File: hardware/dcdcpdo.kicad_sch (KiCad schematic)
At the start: 22 parts, among them J501 MANUAL, U301 SiC437

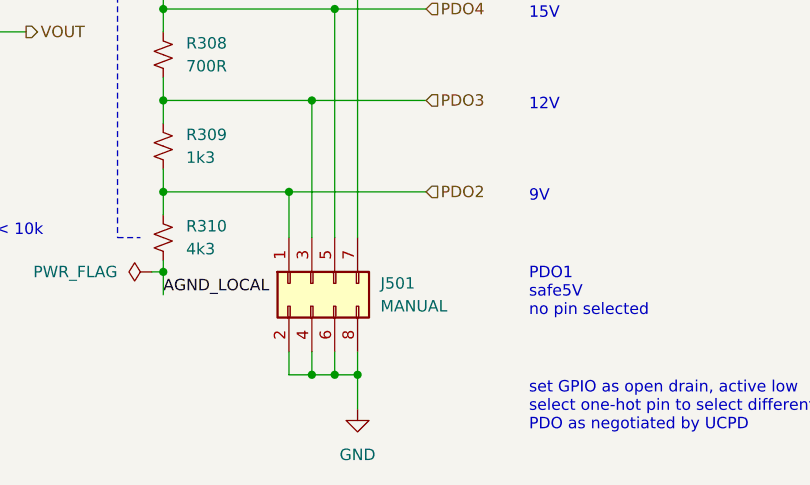
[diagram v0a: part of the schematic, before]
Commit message: Fix SiC437 footprint and LCSC field error
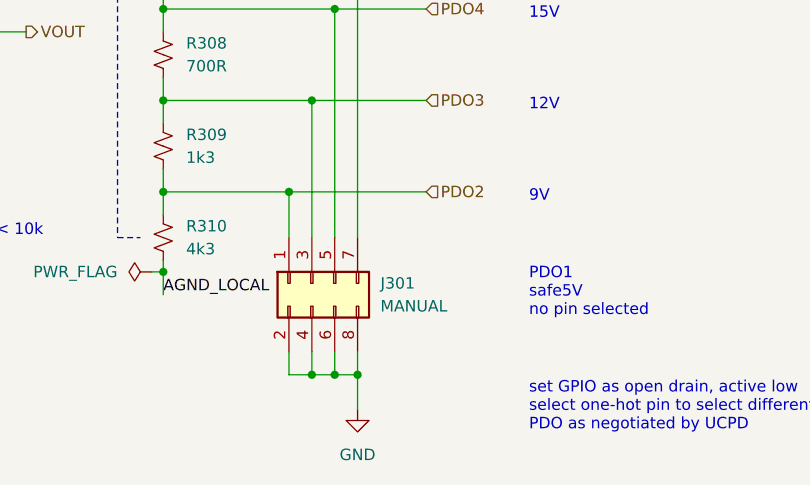
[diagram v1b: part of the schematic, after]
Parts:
- C301, C303: LCSC ID (none) -> C14663; LCSC Part C14663 -> (none)
- C302: LCSC ID (none) -> C45783; LCSC Part C45783 -> (none)
- C304: LCSC ID (none) -> C15849; LCSC Part C15849 -> (none)
- C305: LCSC ID (none) -> C19666; LCSC Part C19666 -> (none)
- C306, C307, C308, C309: LCSC ID (none) -> C76659; LCSC Part C76659 -> (none)
- J301: renamed from J501; LCSC ID (none) -> C2685182
- L301: LCSC ID (none) -> C524588; LCSC Part C524588 -> (none)
- R301: LCSC ID (none) -> C22939; LCSC Part C22939 -> (none)
- R302: LCSC ID (none) -> C25744; LCSC Part C25744 -> (none)
- R303: LCSC ID (none) -> C137971; LCSC Part C137971 -> (none)
- R304: LCSC ID (none) -> C25741; LCSC Part C25741 -> (none)
- R305: LCSC ID (none) -> C25794; LCSC Part C25794 -> (none)
- R306: LCSC ID (none) -> C4109; LCSC Part C4109 -> (none)
- R307, R308: LCSC ID (none) -> C728428; LCSC Part C728428 -> (none)
- R309: LCSC ID (none) -> C25866; LCSC Part C25866 -> (none)
- R310: LCSC ID (none) -> C25899; LCSC Part C25899 -> (none)
- U301: footprint easyeda2kicad:MLP44-24_L4.0-W4.0-P0.45-TL-EP -> matei:SiC437AED; JLCPCB Part # C2071432 -> (none); LCSC ID (none) -> C2071432; LCSC Part C2071432 -> (none)
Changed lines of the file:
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@@
 			)
 		)
-		(property "LCSC Part" "C19666"
+		(property "LCSC ID" "C19666"
 			(at 104.14 102.87 0)
 			(effects
@@
 			)
 		)
-		(property "LCSC Part" "C15849"
+		(property "LCSC ID" "C15849"
 			(at 154.94 62.23 0)
 			(effects
@@
 			)
 		)
-		(property "LCSC Part" "C137971"
+		(property "LCSC ID" "C137971"
 			(at 143.51 49.53 0)
 			(effects
@@
 			)
 		)
-		(property "LCSC Part" "C76659"
+		(property "LCSC ID" "C76659"
 			(at 162.56 102.87 0)
 			(effects
@@
 			)
 		)
-		(property "LCSC Part" "C25899"
+		(property "LCSC ID" "C25899"
 			(at 191.77 120.65 0)
 			(effects
@@
 			)
 		)
-		(property "LCSC Part" "C25866"
+		(property "LCSC ID" "C25866"
 			(at 191.77 110.49 0)
 			(effects
@@
 			)
 		)
-		(property "LCSC Part" "C76659"
+		(property "LCSC ID" "C76659"
 			(at 142.24 102.87 0)
 			(effects
@@
 			)
 		)
-		(property "LCSC Part" "C524588"
+		(property "LCSC ID" "C524588"
 			(at 120.65 97.79 0)
 			(effects
@@
 			)
 		)
-		(property "LCSC Part" "C25744"
+		(property "LCSC ID" "C25744"
 			(at 148.59 43.18 0)
 			(effects
@@
 			)
 		)
-		(property "LCSC Part" "C22939"
+		(property "LCSC ID" "C22939"
 			(at 105.41 36.83 0)
 			(effects
@@
 		(on_board yes)
 		(dnp no)
-		(property "Reference" "J501"
+		(property "Reference" "J301"
 			(at 215.9 125.73 90)
 			(effects
@@
 			)
 		)
+		(property "LCSC ID" "C2685182"
+			(at 208.28 125.73 0)
+			(effects
+				(font
+					(size 1.27 1.27)
+				)
+				(hide yes)
+			)
+		)
 		(pin "2"
 		)
@@
 		(instances
 			(project "pdcard"
+				(path "/a04d6ea3-43ae-48a1-85c5-5c91a24cd719/348037e6-65f2-44d8-8d3f-10d87c91dfbf/93e043fd-2a5d-44fd-a1dc-d2f6639621cc"
+					(reference "J301")
+					(unit 1)
+				)
 				(path "/a04d6ea3-43ae-48a1-85c5-5c91a24cd719/3829ccac-a87e-4e02-8de9-236dec2bccc3/93e043fd-2a5d-44fd-a1dc-d2f6639621cc"
 					(reference "J501")
-					(unit 1)
-				)
-				(path "/a04d6ea3-43ae-48a1-85c5-5c91a24cd719/348037e6-65f2-44d8-8d3f-10d87c91dfbf/93e043fd-2a5d-44fd-a1dc-d2f6639621cc"
-					(reference "J301")
 					(unit 1)
 				)
@@
 			)
 		)
-		(property "LCSC Part" "C76659"
+		(property "LCSC ID" "C76659"
 			(at 152.4 102.87 0)
 			(effects
@@
 			)
 		)
-		(property "LCSC Part" "C25794"
+		(property "LCSC ID" "C25794"
 			(at 166.37 80.01 0)
 			(effects
@@
 			)
 		)
-		(property "Footprint" "easyeda2kicad:MLP44-24_L4.0-W4.0-P0.45-TL-EP"
+		(property "Footprint" "matei:SiC437AED"
 			(at 86.36 49.53 0)
 			(effects
@@
 			)
 		)
-		(property "JLCPCB Part #" "C2071432"
-			(at 113.03 62.23 0)
-			(effects
-				(font
-					(size 1.27 1.27)
-				)
-				(hide yes)
-			)
-		)
-		(property "LCSC Part" "C2071432"
+		(property "LCSC ID" "C2071432"
 			(at 113.03 62.23 0)
 			(effects
@@
 			)
 		)
-		(property "LCSC Part" "C14663"
+		(property "LCSC ID" "C14663"
 			(at 80.01 59.69 0)
 			(effects
@@
 			)
 		)
-		(property "LCSC Part" "C728428"
+		(property "LCSC ID" "C728428"
 			(at 191.77 100.33 0)
 			(effects
@@
 			)
 		)
-		(property "LCSC Part" "C25741"
+		(property "LCSC ID" "C25741"
 			(at 143.51 62.23 0)
 			(effects
@@
 			)
 		)
-		(property "LCSC Part" "C14663"
+		(property "LCSC ID" "C14663"
 			(at 113.03 36.83 0)
 			(effects
@@
 			)
 		)
-		(property "LCSC Part" "C76659"
+		(property "LCSC ID" "C76659"
 			(at 132.08 102.87 0)
 			(effects
@@
 			)
 		)
-		(property "LCSC Part" "C728428"
+		(property "LCSC ID" "C728428"
 			(at 191.77 90.17 0)
 			(effects
@@
 			)
 		)
-		(property "LCSC Part" "C45783"
+		(property "LCSC ID" "C45783"
 			(at 64.77 59.69 0)
 			(effects
@@
 			)
 		)
-		(property "LCSC Part" "C4109"
+		(property "LCSC ID" "C4109"
 			(at 191.77 80.01 0)
 			(effects

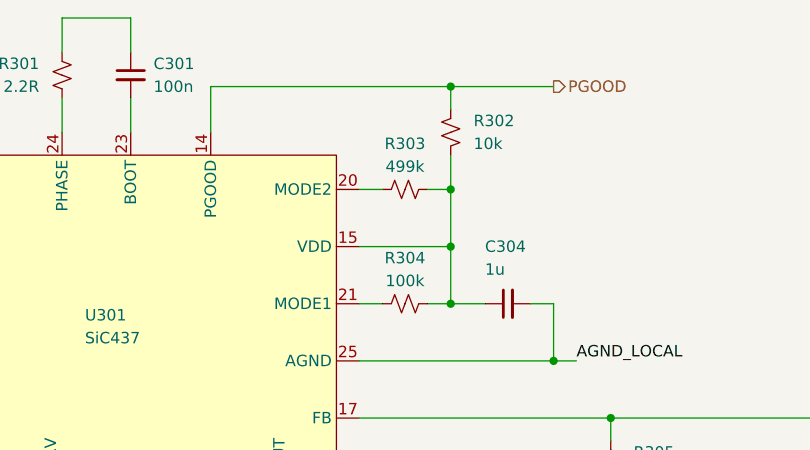
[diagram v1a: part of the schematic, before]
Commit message: change to C8U3 variant
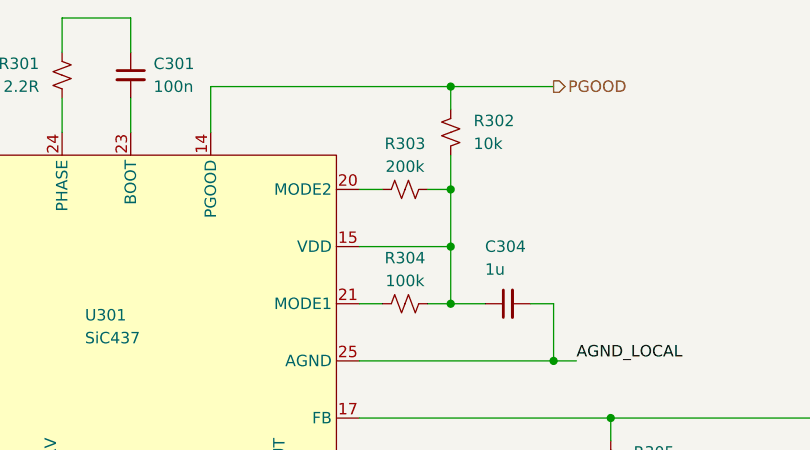
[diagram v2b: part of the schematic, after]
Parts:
- R303: value 499k -> 200k; LCSC ID C137971 -> C25764
